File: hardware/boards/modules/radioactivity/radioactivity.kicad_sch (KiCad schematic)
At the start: 51 parts, among them J1 jmp1, J2 Programming Header, J3 jmp1, Q1 S8050, Q2 MMBTA42, Q3 S8050, Q4 S8050, T1 74LVC1G17GW, U1 TLC555, U2 TLC555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

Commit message: finished geiger module pcb
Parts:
- 100R1: footprint (none) -> common:SMD_3P_3.8X3.6
- C1, C2: footprint (none) -> common:C_Elec_SMD_5x5.4
- C10, C5, C9: footprint (none) -> common:C_1206
- C11, C12, C3, C4, C6, C7, C8, L2: footprint (none) -> common:C_0603
- D1: footprint (none) -> common:LED_0603
- D2, D3, D4: footprint (none) -> common:SMA(DO-214AC)
- G1: footprint (none) -> geiger:Geiger_Tube_J305
- G3: footprint (none) -> air_sens_foots:GPIO_HEADER
- J1: footprint (none) -> common:Jumper_2
- J2: footprint (none) -> air_sens_foots:ATtiny_Programming_Header
- J3: footprint (none) -> common:Jumper_2; now in the parts list
- L1: footprint (none) -> common:SMD(7.1x6.6)
- Q1, Q2, Q3, Q4: footprint (none) -> common:SOT-23
- R1, R10, R11, R12, R13, R14, R15, R16, R17, R2, R3, R4, R5, R6, R7, R8, R9: footprint (none) -> common:R_0603
- S1: footprint (none) -> common:buzzer_8.5x8.5
- T1: footprint (none) -> common:SOT353
- U1, U2: footprint (none) -> common:SOIC-8
- U3: footprint (none) -> air_sens_foots:ATtiny1614
- g2: footprint (none) -> air_sens_foots:gpio_1; now in the parts list

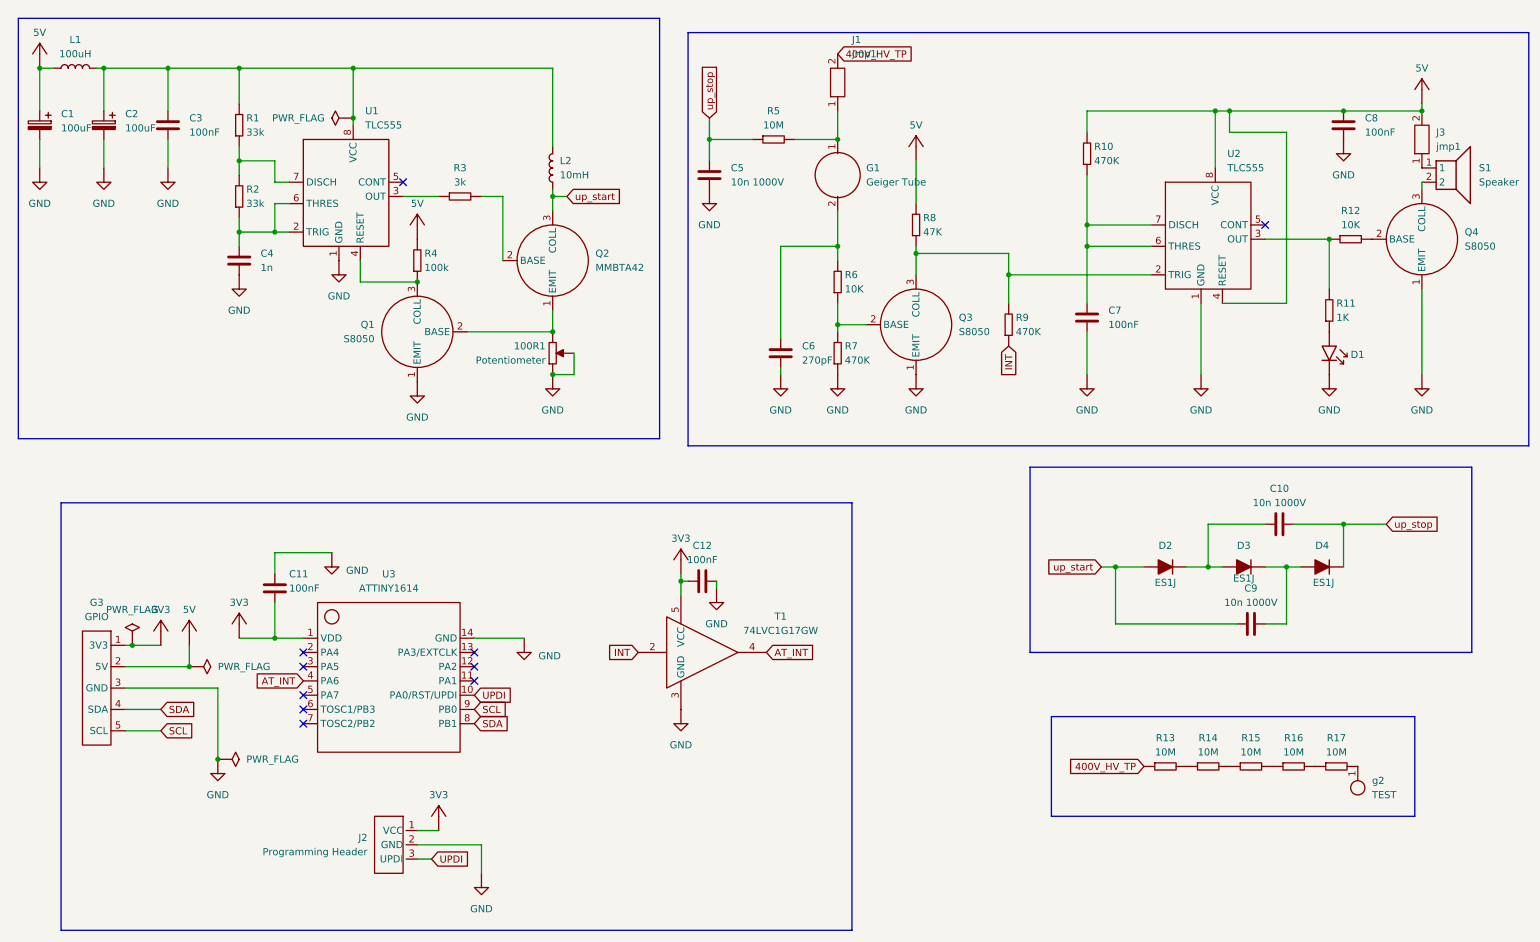
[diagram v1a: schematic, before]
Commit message: added missing status LED to radioactivity board
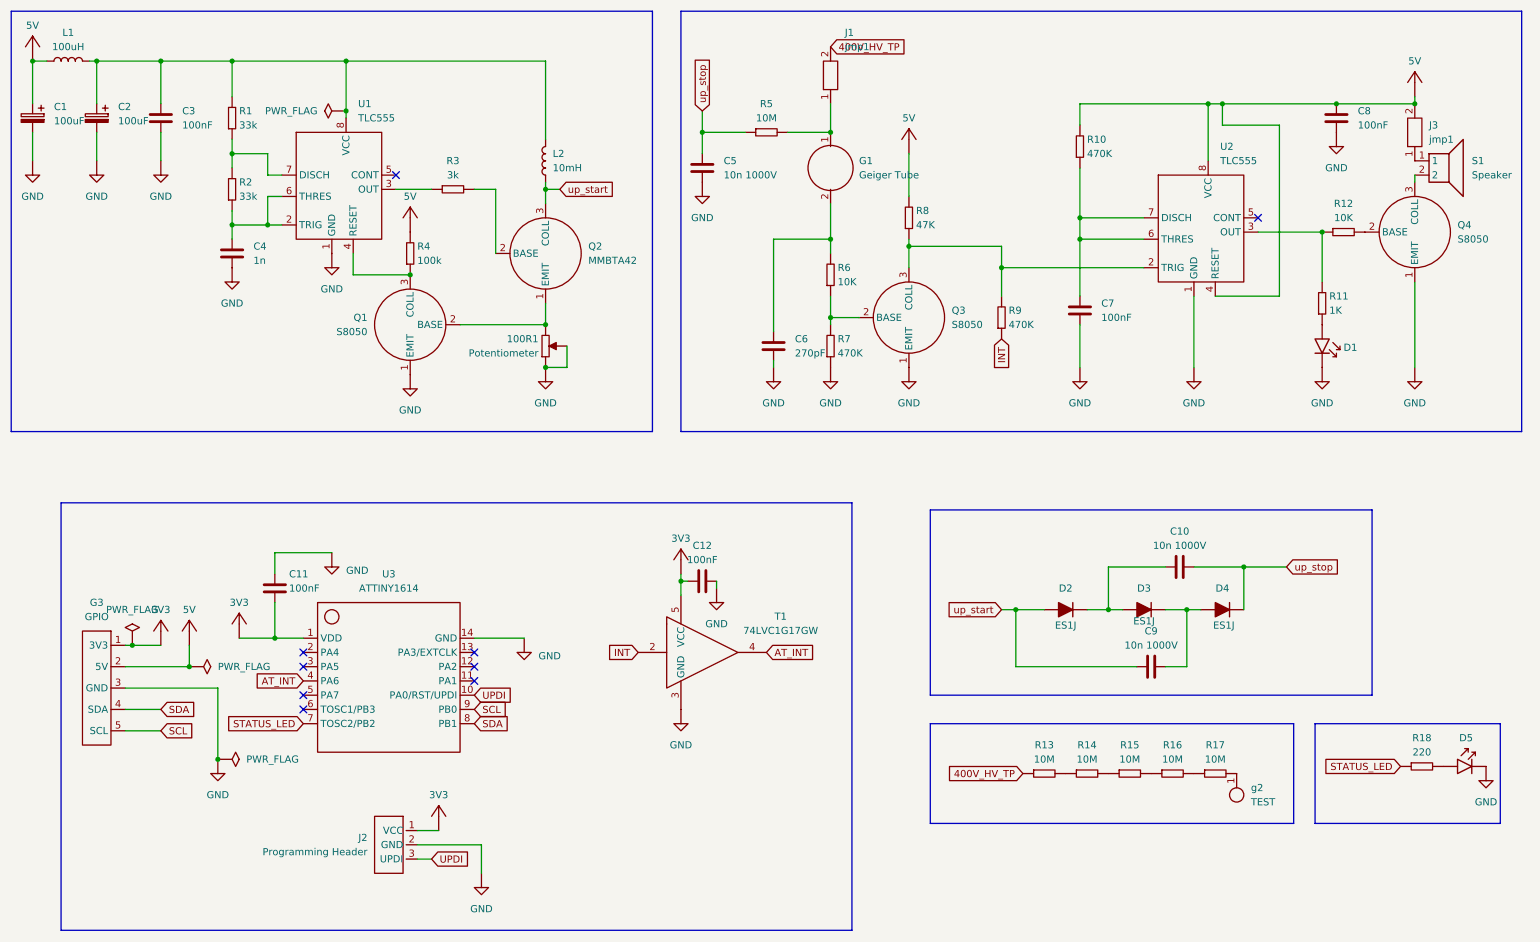
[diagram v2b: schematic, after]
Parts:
- added D5: ~, common:LED_3mm_THT, symbol common:LED
- added R18: 220, common:R_0603, symbol common:Resistor
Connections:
- net GND: now also D5.1 (K)
- net STATUS_LED: now reaches U3.7 (TOSC2/PB2)
- net STATUS_LED: now also R18.1
- new net: D5.2 (A), R18.2
- no-connect marks 10 -> 9
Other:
- moved on the sheet: 100R1, C1, C10, C2, C3, C4, C5, C6, C7, C8, C9, D1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

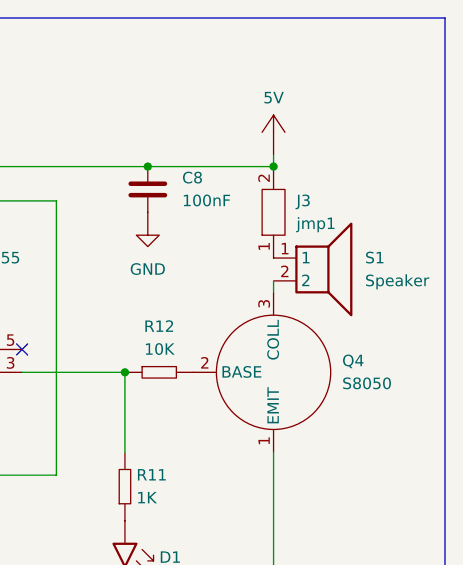
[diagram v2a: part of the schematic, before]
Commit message: updated sensor module schematics
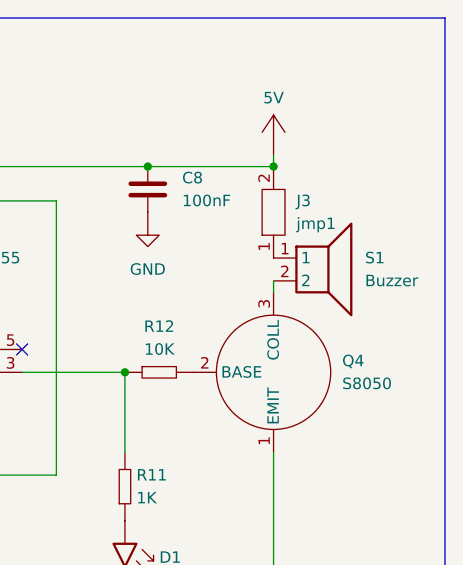
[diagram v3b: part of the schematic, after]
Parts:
- S1: value Speaker -> Buzzer
